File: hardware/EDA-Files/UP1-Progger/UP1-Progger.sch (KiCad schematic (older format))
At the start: 11 parts, among them J1 KUPS-Conn, J2 USB_B_Micro, J3 USB_B, J4 SWD_Interface, J5 ST Link V2 Clone, J6 USB_2.54, SW1 Reset, SW2 Bootsel, U1 LDO_3V3_SOT23-3

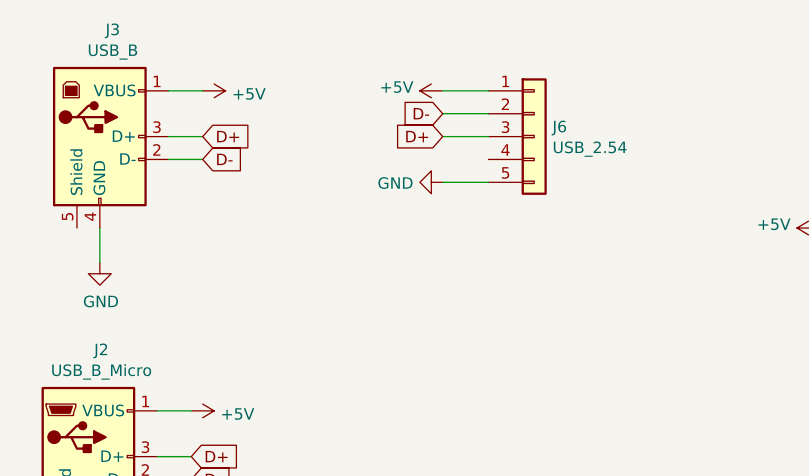
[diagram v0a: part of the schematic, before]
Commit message: made one-sided Progger ready for SMT assembly of USB and LDO V00.20 - not released
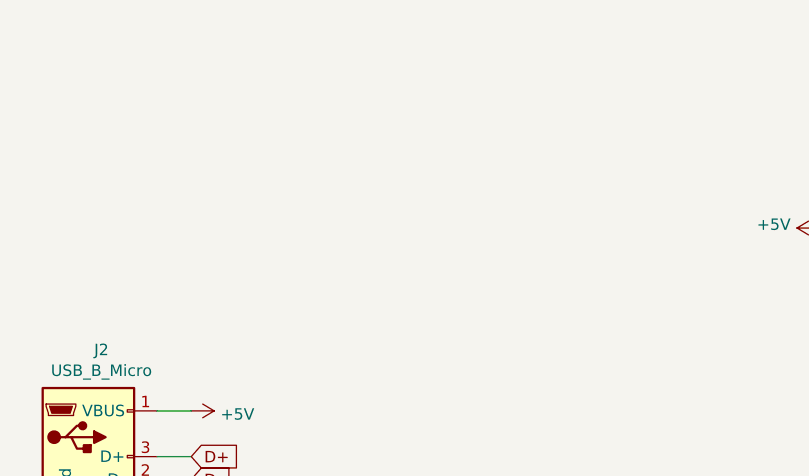
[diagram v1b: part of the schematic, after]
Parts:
- removed J3: USB_B, sirsydom:USB_B_OST_USB-B1HSxx_Horizontal, symbol Connector:USB_B
- removed J6: USB_2.54, Connector_PinHeader_2.54mm:PinHeader_1x05_P2.54mm_Vertical, symbol Connector_Generic:Conn_01x05
- C1, C2: footprint Capacitor_SMD:C_1206_3216Metric_Pad1.42x1.75mm_HandSolder -> Capacitor_SMD:C_0603_1608Metric_Pad1.05x0.95mm_HandSolder
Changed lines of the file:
@@
 EESchema Schematic File Version 4
+LIBS:UP1-Progger-cache
 EELAYER 30 0
 EELAYER END
@@
 Sheet 1 1
 Title "UP1-Progger"
-Date "2022-02-10"
-Rev "V00.10"
+Date "2022-03-06"
+Rev "V00.20"
 Comp "OpenKNX"
 Comment1 "by SirSydom <com@sirsydom.de>"
@@
 F 0 "C2" H 6465 2146 50  0000 L CNN
 F 1 "1uF" H 6465 2055 50  0000 L CNN
-F 2 "Capacitor_SMD:C_1206_3216Metric_Pad1.42x1.75mm_HandSolder" H 6388 1950 50  0001 C CNN
+F 2 "Capacitor_SMD:C_0603_1608Metric_Pad1.05x0.95mm_HandSolder" H 6388 1950 50  0001 C CNN
 F 3 "~" H 6350 2100 50  0001 C CNN
 	1    6350 2100
@@
 F 0 "C1" H 5515 2146 50  0000 L CNN
 F 1 "1uF" H 5515 2055 50  0000 L CNN
-F 2 "Capacitor_SMD:C_1206_3216Metric_Pad1.42x1.75mm_HandSolder" H 5438 1950 50  0001 C CNN
+F 2 "Capacitor_SMD:C_0603_1608Metric_Pad1.05x0.95mm_HandSolder" H 5438 1950 50  0001 C CNN
 F 3 "~" H 5400 2100 50  0001 C CNN
 	1    5400 2100
@@
 $EndComp
 $Comp
-L Connector:USB_B J3
-U 1 1 607B278B
-P 2150 1550
-F 0 "J3" H 2207 2017 50  0000 C CNN
-F 1 "USB_B" H 2207 1926 50  0000 C CNN
-F 2 "sirsydom:USB_B_OST_USB-B1HSxx_Horizontal" H 2300 1500 50  0001 C CNN
-F 3 " ~" H 2300 1500 50  0001 C CNN
-	1    2150 1550
-	1    0    0    -1
-$EndComp
-$Comp
-L power:GND #PWR0107
-U 1 1 607B36B9
-P 2150 2100
-F 0 "#PWR0107" H 2150 1850 50  0001 C CNN
-F 1 "GND" H 2155 1927 50  0000 C CNN
-F 2 "" H 2150 2100 50  0001 C CNN
-F 3 "" H 2150 2100 50  0001 C CNN
-	1    2150 2100
-	1    0    0    -1
-$EndComp
-Wire Wire Line
-	2150 2100 2150 1950
-$Comp
-L power:+5V #PWR0108
-U 1 1 607B3FA9
-P 2600 1350
-F 0 "#PWR0108" H 2600 1200 50  0001 C CNN
-F 1 "+5V" V 2615 1478 50  0000 L CNN
-F 2 "" H 2600 1350 50  0001 C CNN
-F 3 "" H 2600 1350 50  0001 C CNN
-	1    2600 1350
-	0    1    1    0
-$EndComp
-Text GLabel 2600 1650 2    50   Input ~ 0
-D-
-Text GLabel 2600 1550 2    50   Input ~ 0
-D+
-Wire Wire Line
-	2600 1350 2450 1350
-Wire Wire Line
-	2450 1550 2600 1550
-Wire Wire Line
-	2600 1650 2450 1650
-$Comp
 L Connector:USB_B_Micro J2
 U 1 1 607B5533
@@
 	3100 5700 2900 5700
 $Comp
-L Connector_Generic:Conn_01x05 J6
-U 1 1 607C77D8
-P 4050 1550
-F 0 "J6" H 4130 1592 50  0000 L CNN
-F 1 "USB_2.54" H 4130 1501 50  0000 L CNN
-F 2 "Connector_PinHeader_2.54mm:PinHeader_1x05_P2.54mm_Vertical" H 4050 1550 50  0001 C CNN
-F 3 "~" H 4050 1550 50  0001 C CNN
-	1    4050 1550
-	1    0    0    -1
-$EndComp
-$Comp
-L power:+5V #PWR0117
-U 1 1 607D3379
-P 3650 1350
-F 0 "#PWR0117" H 3650 1200 50  0001 C CNN
-F 1 "+5V" V 3665 1478 50  0000 L CNN
-F 2 "" H 3650 1350 50  0001 C CNN
-F 3 "" H 3650 1350 50  0001 C CNN
-	1    3650 1350
-	0    -1   -1   0
-$EndComp
-Text GLabel 3650 1450 0    50   Input ~ 0
-D-
-Text GLabel 3650 1550 0    50   Input ~ 0
-D+
-$Comp
-L power:GND #PWR0118
-U 1 1 607D3B0F
-P 3650 1750
-F 0 "#PWR0118" H 3650 1500 50  0001 C CNN
-F 1 "GND" V 3655 1622 50  0000 R CNN
-F 2 "" H 3650 1750 50  0001 C CNN
-F 3 "" H 3650 1750 50  0001 C CNN
-	1    3650 1750
-	0    1    1    0
-$EndComp
-Wire Wire Line
-	3650 1350 3850 1350
-Wire Wire Line
-	3850 1450 3650 1450
-Wire Wire Line
-	3650 1550 3850 1550
-Wire Wire Line
-	3850 1750 3650 1750
-$Comp
 L Switch:SW_Push SW1
